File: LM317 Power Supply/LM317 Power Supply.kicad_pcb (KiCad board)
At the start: 2 copper layers, 41.9 x 40.6 mm, 23 parts, among them CON1 BARREL_JACK, K1 CONN_3, U1 LM317, U2 LT1206

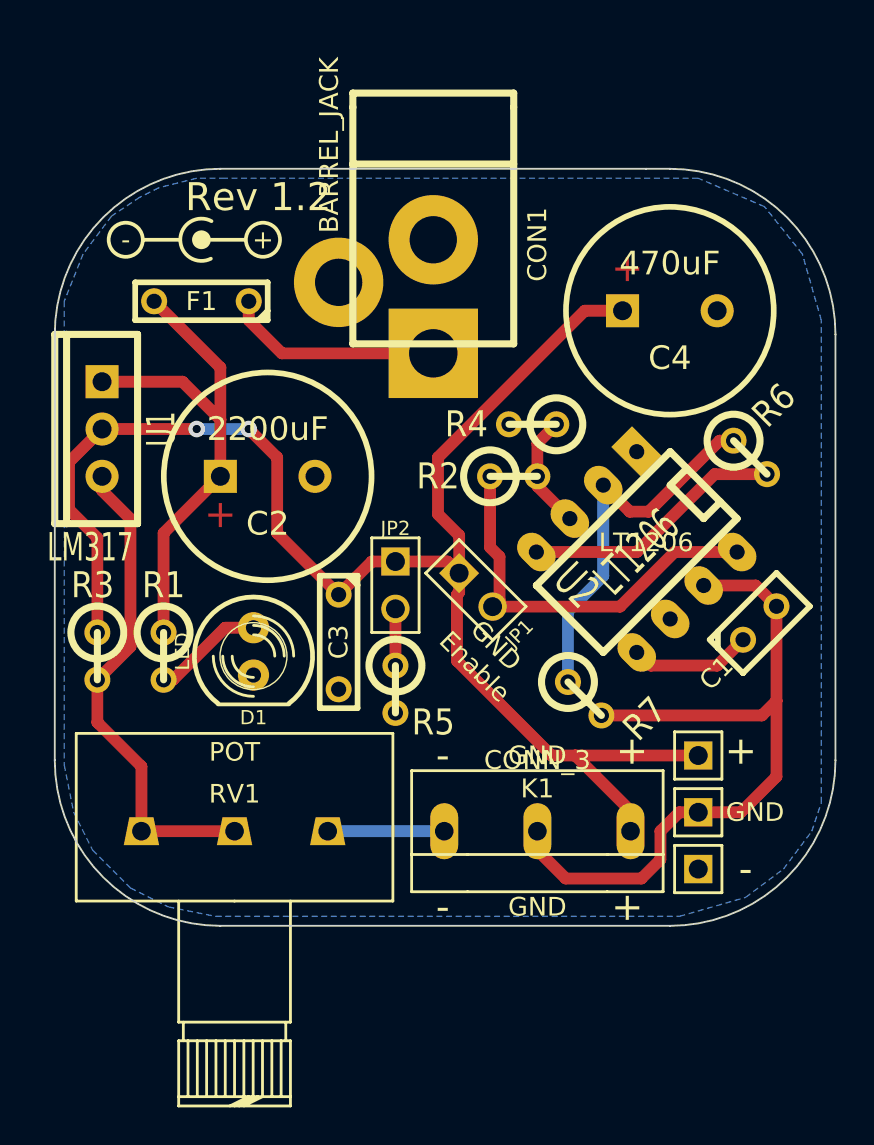
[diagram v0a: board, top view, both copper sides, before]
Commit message: Power Supply Rev 1.3
Deleted unnecesary load, fixed potentiometer orientation and other stuff
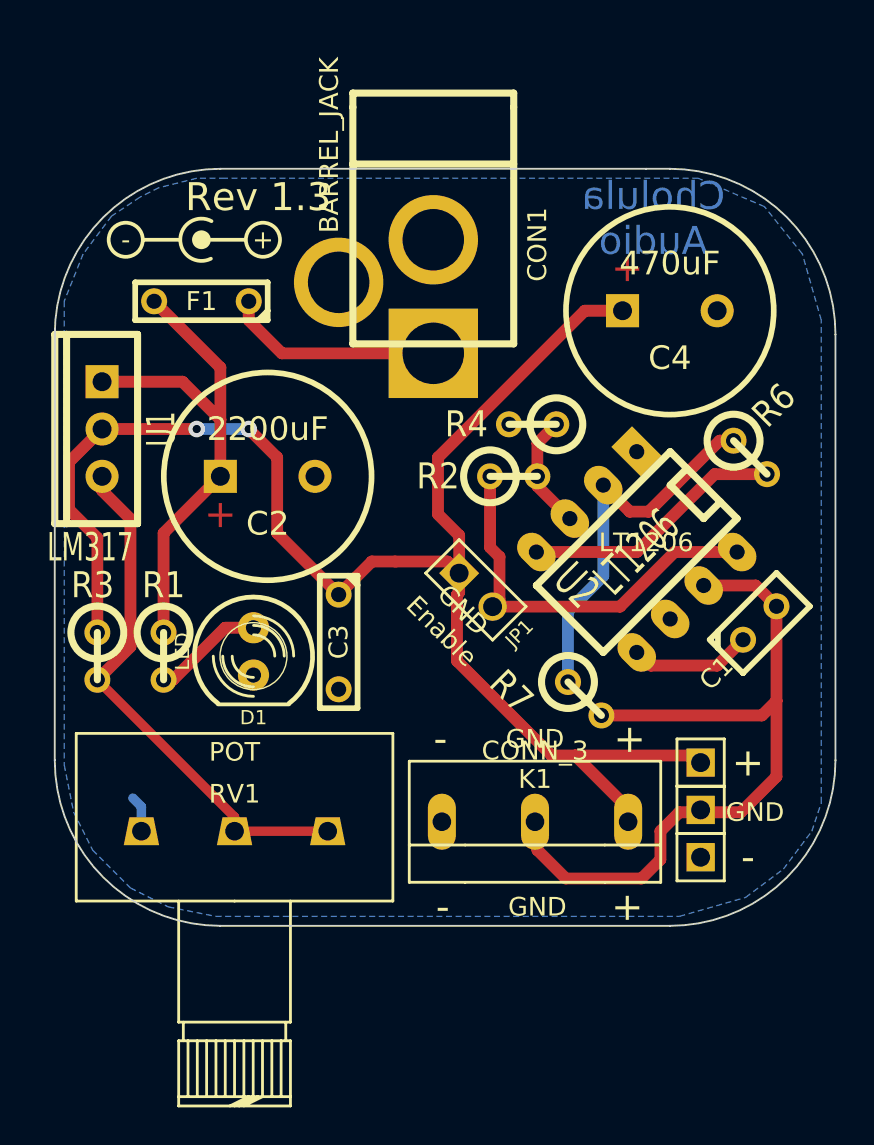
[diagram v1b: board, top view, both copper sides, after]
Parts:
- removed JP2: JUMPER, PIN_ARRAY_2X1
- removed R5: 1k, R1
- R3: value 120 -> 240
- moved TP3 0.65 mm to (155.6, 103.5)
- moved K1 0.52 mm to (146.7, 101.6)
- moved TP1 0.40 mm to (155.6, 98.4)
- moved TP2 0.18 mm to (155.6, 101.0)
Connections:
- R3 pad 2: N-0000013 -> N-0000011
- RV1 pad 1: N-0000013 -> /V-
- RV1 pad 2: N-0000013 -> N-0000011
- RV1 pad 3: /V- -> N-0000011
- U1 pad 2: N-0000013 -> N-0000011
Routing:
- net N-0000011: track 0.00 -> 28.5 mm
- net N-0000013: track 26.4 -> 0.00 mm
- net /V-: track 6.26 -> 1.97 mm
- net N-000004 (its old number): track 3.05 -> 0.00 mm
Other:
- board text added: "Cholula Audio"
- board text added: "Rev 1.3"
- board text removed: "By Diego R"
- board text removed: "Rev 1.2"
